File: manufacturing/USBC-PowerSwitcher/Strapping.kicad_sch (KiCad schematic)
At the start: 13 parts, among them J2 SWD, Y1 16MHz xpF

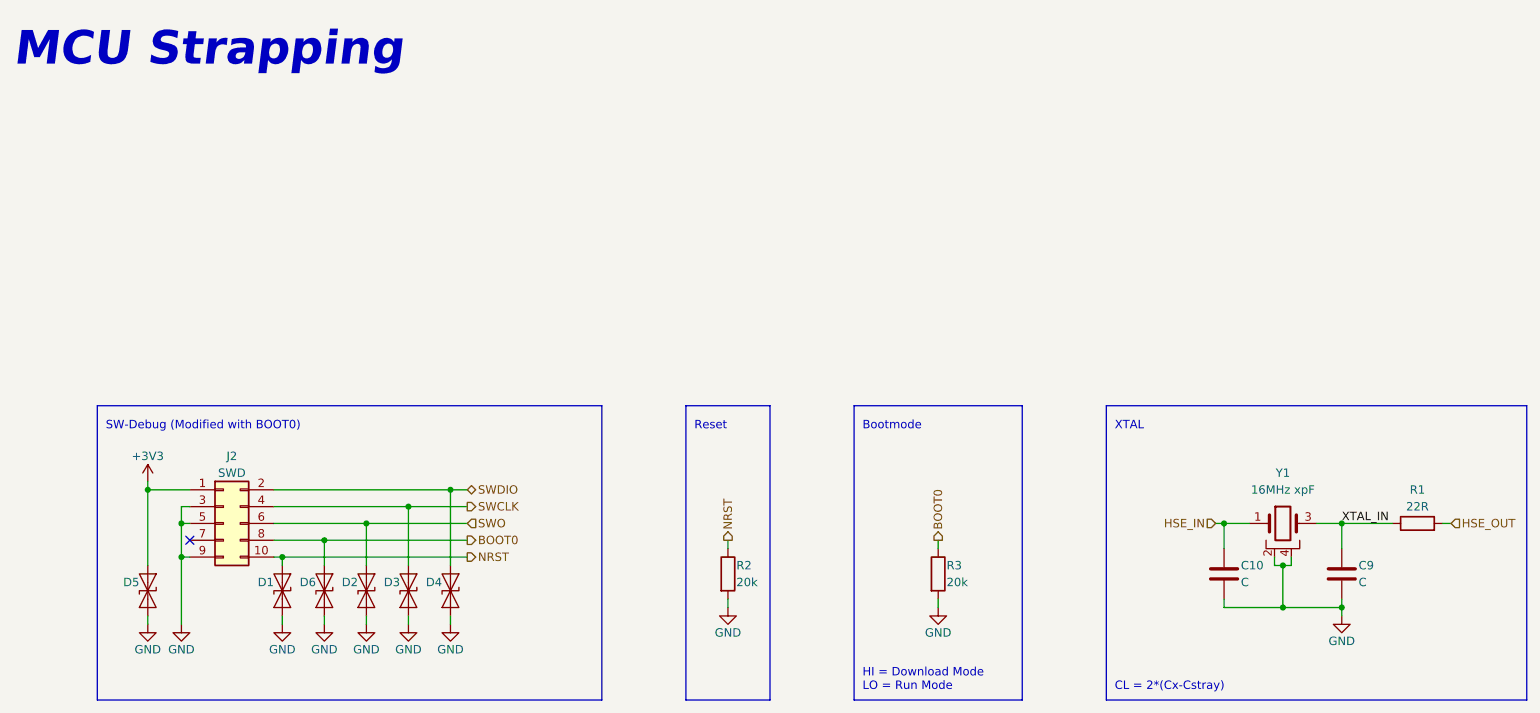
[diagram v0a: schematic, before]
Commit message: First Rough placement
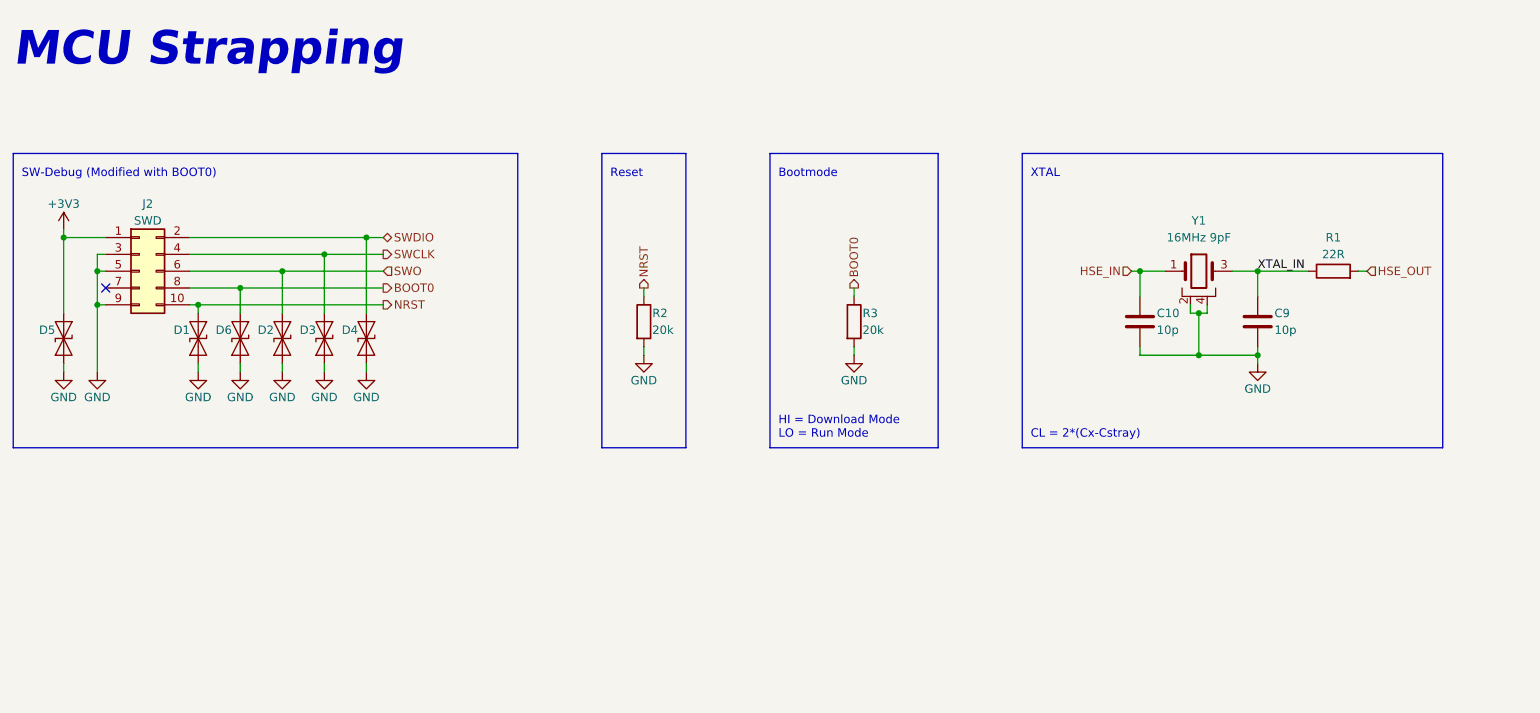
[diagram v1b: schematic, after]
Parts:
- C10, C9: value C -> 10p; footprint (none) -> Capacitor_SMD:C_0402_1005Metric; LCSC # (none) -> C32949
- D1, D2, D3, D4, D5, D6: LCSC # (none) -> C96512
- J2: footprint (none) -> Connector_PinHeader_2.54mm:PinHeader_2x05_P2.54mm_Horizontal
- R1: footprint (none) -> Resistor_SMD:R_0402_1005Metric; LCSC # (none) -> C25092
- R2, R3: footprint (none) -> Resistor_SMD:R_0402_1005Metric; LCSC # (none) -> C25765
- Y1: value 16MHz xpF -> 16MHz 9pF; footprint (none) -> Crystal:Crystal_SMD_3225-4Pin_3.2x2.5mm; LCSC # (none) -> C13738
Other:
- moved on the sheet: C10, C9, D1, D2, D3, D4, D5, D6, J2, R1, R2, R3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
